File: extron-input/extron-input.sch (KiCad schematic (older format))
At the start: 20 parts, among them J1 SCART-F, J10 Conn_01x01, J11 Conn_01x01, J2 RED, J3 GREEN, J4 BLUE, J5 SYNC, J6 PHOENIX, J7 SENSE, J8 Conn_01x01, J9 Conn_01x01, SW1 SW_DPDT_x2, U1 LM1881

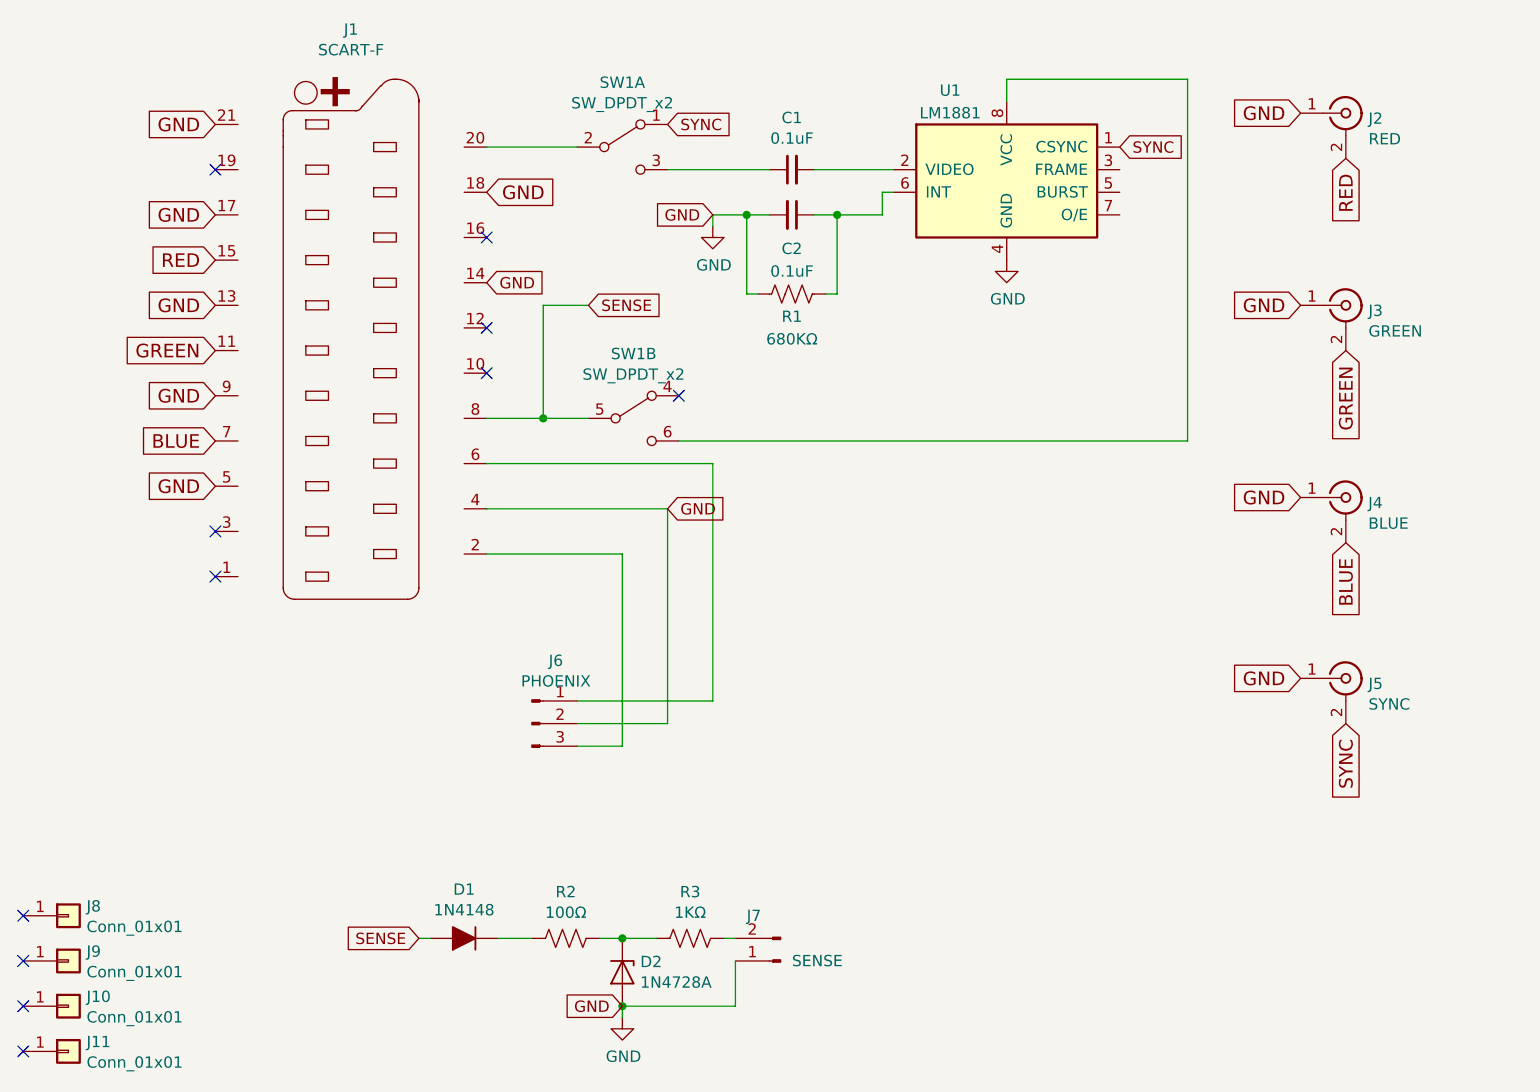
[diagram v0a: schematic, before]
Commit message: Version 3.1 (#6)
* WIP on input board v3

New features:
  Longer boards that support top/bottom placement, allowing closer
  placement for extron 300 ADSP models, and allowing thicker FR4 again

  Will have new RCA placements to support both older and newer extron
  BNC spacings

* WIP v3 (more)

* Made separate top/bottom directories (only top for now)
* Made symlinks to keep one schematic for two pcbs
* Modified "rca_combined" to no longer be combined. We're going w/ the rca
  boom from lcsc.
* Doubled up footprints for R / B / Sync to support both new and old
  extron crosspoints

* Added bottom board

* Changed top to 45 degree scart insertion

I've also aligned the mounting holes between the boards

* Found a size for the bottom board that won't impede on the top board

* extron-input v3

Extended bottom board by 5mm
Fixed silkscreen up to be reasonable
Fixed up gitignore

Still need to clean up base output directory. Will happend when bottom
output board is done.

* Add bottom output board

* Cleanup towards better top/bottom output board file hierarchy

* Updated renders and added a bit more docs for input cards

* Add a bit of extron-output readme update (renders)

* Fix bottom 3d side render

* New layout renders

* More readme fixes

* More readme

* Redo renders, update PCB 3d models for side connectors

Remove ropeproject, add gitignore to stop adding in the future

* More documentation/images

* Update some images, move traces to make ground flood better

* Replace renders with new top/bottom renders

* Updated extron output readme to reflect correct BOM + prices
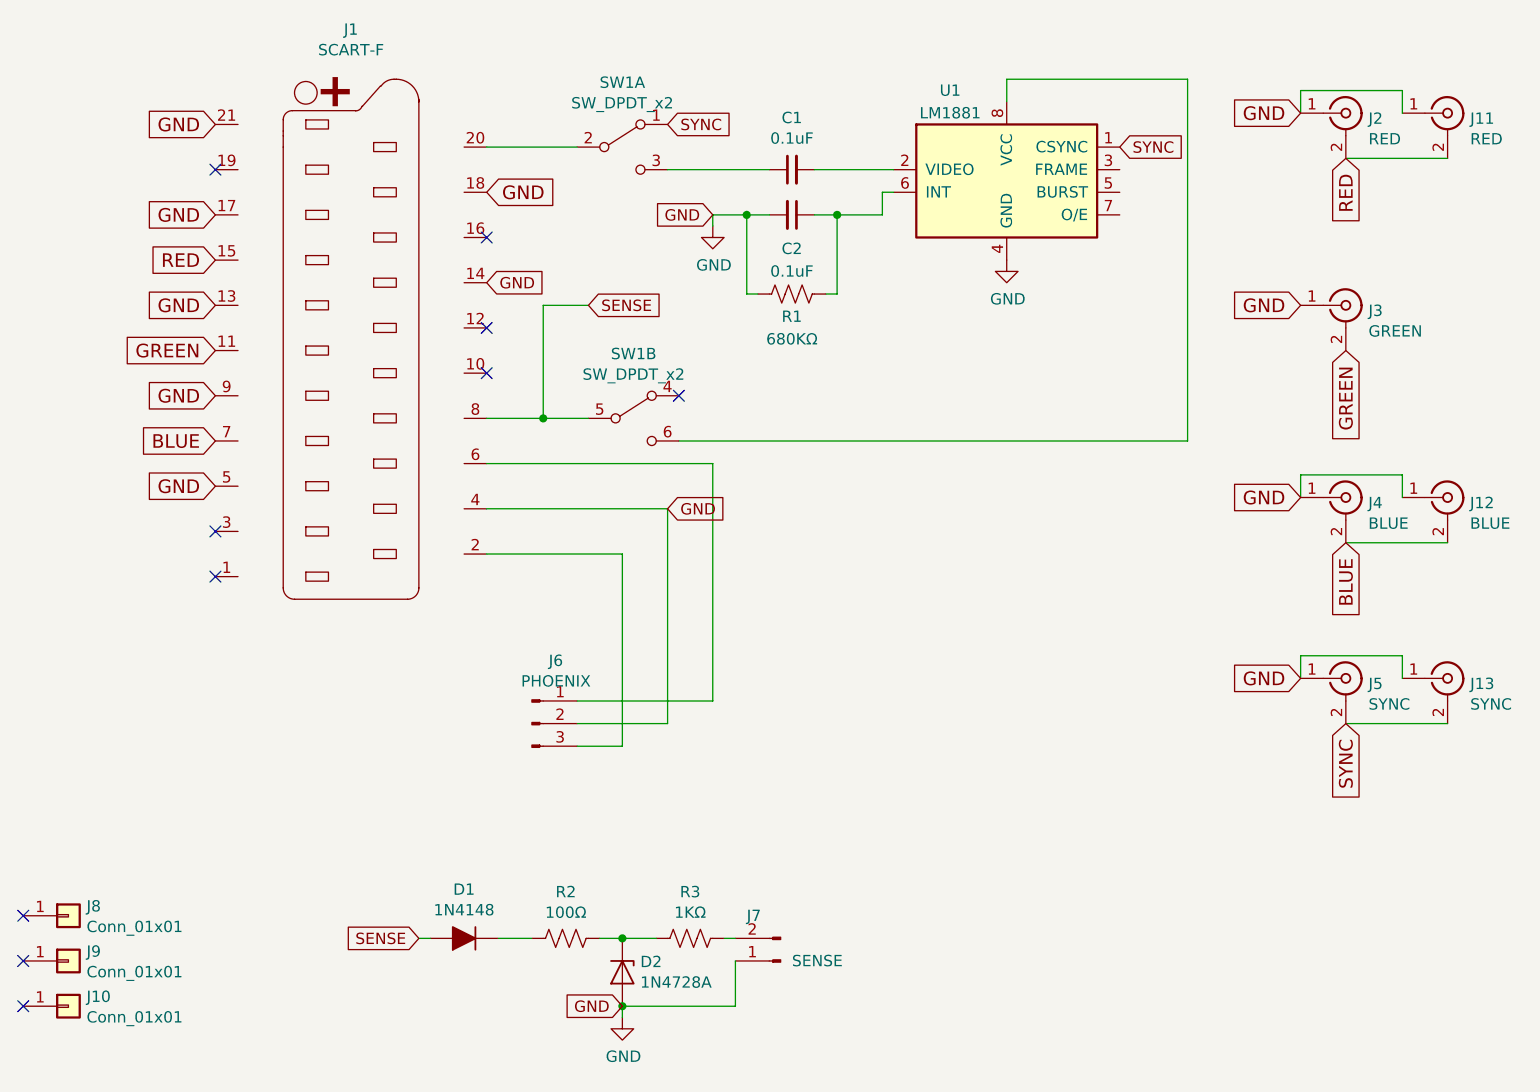
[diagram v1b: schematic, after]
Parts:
- removed J11: Conn_01x01, MountingHole:MountingHole_3.2mm_M3, symbol Connector_Generic:Conn_01x01
- added J11: RED, extron-input:rca_combined, symbol Connector:Conn_Coaxial
- added J12: BLUE, extron-input:rca_combined, symbol Connector:Conn_Coaxial
- added J13: SYNC, extron-input:rca_combined, symbol Connector:Conn_Coaxial
- J6: footprint Connector_JST:JST_XH_S03B-XH-A_1x03_P2.50mm_Horizontal -> Connector_JST:JST_XH_S3B-XH-A-1_1x03_P2.50mm_Horizontal
- J7: footprint Connector_JST:JST_XH_S02B-XH-A_1x02_P2.50mm_Horizontal -> Connector_JST:JST_XH_S2B-XH-A_1x02_P2.50mm_Horizontal
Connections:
- net BLUE: now also J12.2 (Ext)
- net GND: now also J11.1 (In), J12.1 (In), J13.1 (In)
- net RED: now also J11.2 (Ext)
- net SYNC: now also J13.2 (Ext)
- no-connect marks 11 -> 10
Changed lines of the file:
@@
 F 0 "J6" H 4756 5028 50  0000 C CNN
 F 1 "PHOENIX" H 4756 4937 50  0000 C CNN
-F 2 "Connector_JST:JST_XH_S03B-XH-A_1x03_P2.50mm_Horizontal" H 4650 4750 50  0001 C CNN
+F 2 "Connector_JST:JST_XH_S3B-XH-A-1_1x03_P2.50mm_Horizontal" H 4650 4750 50  0001 C CNN
 F 3 "~" H 4650 4750 50  0001 C CNN
 F 4 "https://lcsc.com/product-detail/XH-Connectors_JST_S3B-XH-A-LF-SN_XHsocket-1-3P-Curved-needle-pitch2-5mm_C157928.html" H 4650 4750 50  0001 C CNN "Vendor"
@@
 F 0 "J7" H 5900 5600 50  0000 R CNN
 F 1 "SENSE" H 5700 5800 50  0000 R CNN
-F 2 "Connector_JST:JST_XH_S02B-XH-A_1x02_P2.50mm_Horizontal" H 5750 5800 50  0001 C CNN
+F 2 "Connector_JST:JST_XH_S2B-XH-A_1x02_P2.50mm_Horizontal" H 5750 5800 50  0001 C CNN
 F 3 "~" H 5750 5800 50  0001 C CNN
 F 4 "https://lcsc.com/product-detail/XH-Connectors_JST_S2B-XH-A-LF-SN_XHsocket-1-2P-Curved-needle-pitch2-5mm_C157931.html" H 5750 5800 50  0001 C CNN "Vendor"
@@
 NoConn ~ 2400 5800
 NoConn ~ 2400 6000
-NoConn ~ 2400 6200
 $Comp
 L Connector_Generic:Conn_01x01 J8
@@
 F 3 "~" H 2600 6000 50  0001 C CNN
 	1    2600 6000
-	1    0    0    -1
-$EndComp
-$Comp
-L Connector_Generic:Conn_01x01 J11
-U 1 1 5C7607B9
-P 2600 6200
-F 0 "J11" H 2680 6242 50  0000 L CNN
-F 1 "Conn_01x01" H 2680 6151 50  0000 L CNN
-F 2 "MountingHole:MountingHole_3.2mm_M3" H 2600 6200 50  0001 C CNN
-F 3 "~" H 2600 6200 50  0001 C CNN
-	1    2600 6200
 	1    0    0    -1
 $EndComp
@@
 $EndComp
 $Comp
+L Connector:Conn_Coaxial J4
+U 1 1 5C84997A
+P 8250 3750
+F 0 "J4" H 8349 3726 50  0000 L CNN
+F 1 "BLUE" H 8349 3635 50  0000 L CNN
+F 2 "extron-input:rca_combined" H 8250 3750 50  0001 C CNN
+F 3 " ~" H 8250 3750 50  0001 C CNN
+F 4 "https://lcsc.com/product-detail/AV-Connectors_AV-5_C18080.html" H 8250 3750 50  0001 C CNN "Vendor"
+	1    8250 3750
+	1    0    0    -1
+$EndComp
+$Comp
+L Connector:Conn_Coaxial J5
+U 1 1 5C8499F8
+P 8250 4550
+F 0 "J5" H 8350 4526 50  0000 L CNN
+F 1 "SYNC" H 8350 4435 50  0000 L CNN
+F 2 "extron-input:rca_combined" H 8250 4550 50  0001 C CNN
+F 3 " ~" H 8250 4550 50  0001 C CNN
+F 4 "https://lcsc.com/product-detail/AV-Connectors_AV-5_C18080.html" H 8250 4550 50  0001 C CNN "Vendor"
+	1    8250 4550
+	1    0    0    -1
+$EndComp
+Wire Wire Line
+	5050 4850 4850 4850
+Wire Wire Line
+	5050 4000 5050 4850
+Wire Wire Line
+	5250 4750 4850 4750
+Wire Wire Line
+	5250 3800 5250 4750
+$Comp
+L Switch:SW_DPDT_x2 SW1
+U 2 1 5C75001B
+P 5100 3400
+F 0 "SW1" H 5100 3685 50  0000 C CNN
+F 1 "SW_DPDT_x2" H 5100 3594 50  0000 C CNN
+F 2 "Button_Switch_THT:SW_CuK_JS202011AQN_DPDT_Angled" H 5100 3400 50  0001 C CNN
+F 3 "" H 5100 3400 50  0001 C CNN
+F 4 "https://lcsc.com/product-detail/Toggle-Switches_C-K_JS202011AQN_C-K-JS202011AQN_C221662.html" H 5100 3400 50  0001 C CNN "Vendor"
+	2    5100 3400
+	1    0    0    -1
+$EndComp
+$Comp
+L Connector:Conn_Coaxial J11
+U 1 1 5CF20E44
+P 8700 2050
+F 0 "J11" H 8800 2026 50  0000 L CNN
+F 1 "RED" H 8800 1935 50  0000 L CNN
+F 2 "extron-input:rca_combined" H 8700 2050 50  0001 C CNN
+F 3 " ~" H 8700 2050 50  0001 C CNN
+F 4 "https://lcsc.com/product-detail/AV-Connectors_AV-5_C18080.html" H 8700 2050 50  0001 C CNN "Vendor"
+	1    8700 2050
+	1    0    0    -1
+$EndComp
+$Comp
 L Connector:Conn_Coaxial J3
 U 1 1 5C849928
@@
 $EndComp
 $Comp
-L Connector:Conn_Coaxial J4
-U 1 1 5C84997A
-P 8250 3750
-F 0 "J4" H 8349 3726 50  0000 L CNN
-F 1 "BLUE" H 8349 3635 50  0000 L CNN
-F 2 "extron-input:rca_combined" H 8250 3750 50  0001 C CNN
-F 3 " ~" H 8250 3750 50  0001 C CNN
-F 4 "https://lcsc.com/product-detail/AV-Connectors_AV-5_C18080.html" H 8250 3750 50  0001 C CNN "Vendor"
-	1    8250 3750
-	1    0    0    -1
-$EndComp
-$Comp
-L Connector:Conn_Coaxial J5
-U 1 1 5C8499F8
-P 8250 4550
-F 0 "J5" H 8350 4526 50  0000 L CNN
-F 1 "SYNC" H 8350 4435 50  0000 L CNN
-F 2 "extron-input:rca_combined" H 8250 4550 50  0001 C CNN
-F 3 " ~" H 8250 4550 50  0001 C CNN
-F 4 "https://lcsc.com/product-detail/AV-Connectors_AV-5_C18080.html" H 8250 4550 50  0001 C CNN "Vendor"
-	1    8250 4550
-	1    0    0    -1
-$EndComp
-Wire Wire Line
-	5050 4850 4850 4850
-Wire Wire Line
-	5050 4000 5050 4850
-Wire Wire Line
-	5250 4750 4850 4750
-Wire Wire Line
-	5250 3800 5250 4750
-$Comp
-L Switch:SW_DPDT_x2 SW1
-U 2 1 5C75001B
-P 5100 3400
-F 0 "SW1" H 5100 3685 50  0000 C CNN
-F 1 "SW_DPDT_x2" H 5100 3594 50  0000 C CNN
-F 2 "Button_Switch_THT:SW_CuK_JS202011AQN_DPDT_Angled" H 5100 3400 50  0001 C CNN
-F 3 "" H 5100 3400 50  0001 C CNN
-F 4 "https://lcsc.com/product-detail/Toggle-Switches_C-K_JS202011AQN_C-K-JS202011AQN_C221662.html" H 5100 3400 50  0001 C CNN "Vendor"
-	2    5100 3400
-	1    0    0    -1
-$EndComp
+L Connector:Conn_Coaxial J12
+U 1 1 5CF22661
+P 8700 3750
+F 0 "J12" H 8799 3726 50  0000 L CNN
+F 1 "BLUE" H 8799 3635 50  0000 L CNN
+F 2 "extron-input:rca_combined" H 8700 3750 50  0001 C CNN
+F 3 " ~" H 8700 3750 50  0001 C CNN
+F 4 "https://lcsc.com/product-detail/AV-Connectors_AV-5_C18080.html" H 8700 3750 50  0001 C CNN "Vendor"
+	1    8700 3750
+	1    0    0    -1
+$EndComp
+$Comp
+L Connector:Conn_Coaxial J13
+U 1 1 5CF22C42
+P 8700 4550
+F 0 "J13" H 8800 4526 50  0000 L CNN
+F 1 "SYNC" H 8800 4435 50  0000 L CNN
+F 2 "extron-input:rca_combined" H 8700 4550 50  0001 C CNN
+F 3 " ~" H 8700 4550 50  0001 C CNN
+F 4 "https://lcsc.com/product-detail/AV-Connectors_AV-5_C18080.html" H 8700 4550 50  0001 C CNN "Vendor"
+	1    8700 4550
+	1    0    0    -1
+$EndComp
+Wire Wire Line
+	8250 4750 8700 4750
+Wire Wire Line
+	8050 4550 8050 4450
+Wire Wire Line
+	8050 4450 8500 4450
+Wire Wire Line
+	8500 4450 8500 4550
+Wire Wire Line
+	8050 3750 8050 3650
+Wire Wire Line
+	8050 3650 8500 3650
+Wire Wire Line
+	8500 3650 8500 3750
+Wire Wire Line
+	8250 3950 8700 3950
+Wire Wire Line
+	8500 2050 8500 1950
+Wire Wire Line
+	8500 1950 8050 1950
+Wire Wire Line
+	8050 1950 8050 2050
+Wire Wire Line
+	8250 2250 8700 2250
 $EndSCHEMATC
